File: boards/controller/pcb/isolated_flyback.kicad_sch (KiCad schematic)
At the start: 20 parts, among them T901 150u

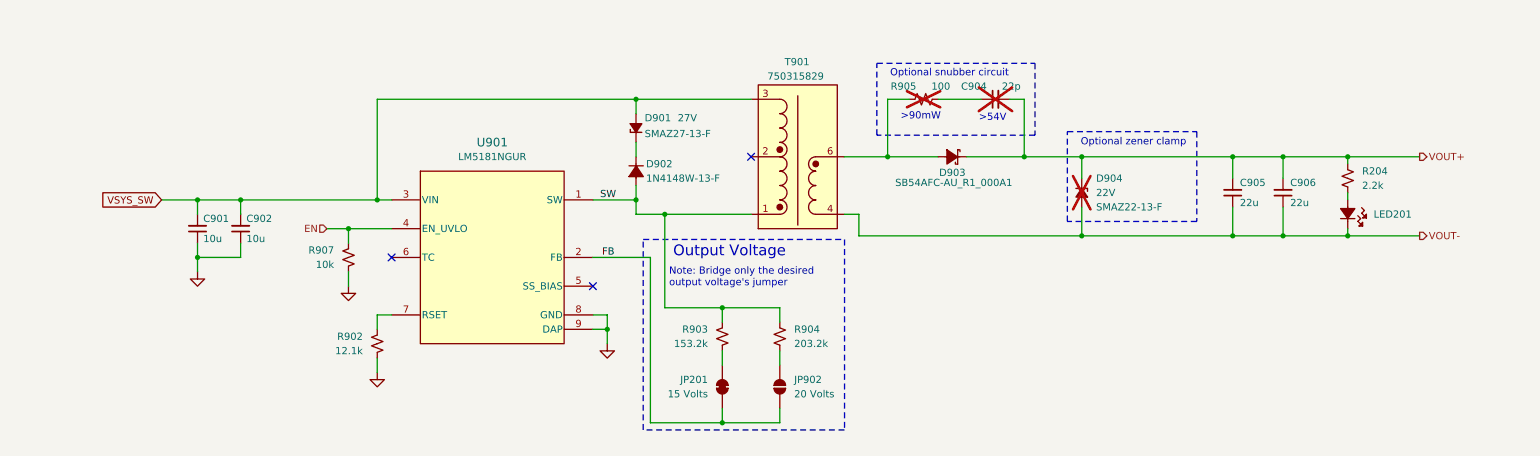
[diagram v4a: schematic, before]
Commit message: controller: pcb: Update schematic
Signed-off-by: Nicholas Loehrke <nicholasnloehrke@gmail.com>
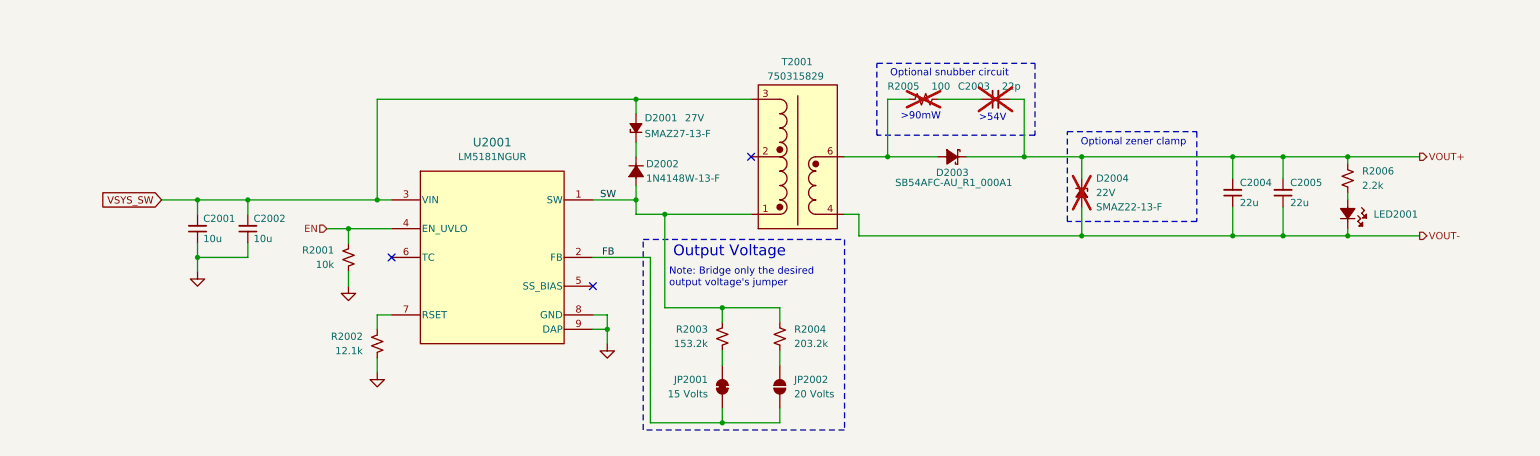
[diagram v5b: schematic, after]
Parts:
- renumbered C901 to C2001, C902 to C2002, C904 to C2003, C905 to C2004, C906 to C2005, D901 to D2001, D902 to D2002, D903 to D2003, D904 to D2004, JP201 to JP2001, JP902 to JP2002, LED201 to LED2001, R907 to R2001, R902 to R2002, R903 to R2003, R904 to R2004, R905 to R2005, R204 to R2006, T901 to T2001, U901 to U2001
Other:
- moved on the sheet: C2002
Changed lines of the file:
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@@
+	)
+	(junction
+		(at 54.61 93.98)
+		(diameter 0)
+		(color 0 0 0 0)
 	)
 	(junction
@@
 	)
 	(junction
-		(at 53.34 93.98)
-		(diameter 0)
-		(color 0 0 0 0)
-	)
-	(junction
 		(at 123.19 93.98)
 		(diameter 0)
@@
 	(wire
 		(pts
-			(xy 53.34 93.98) (xy 77.47 93.98)
-		)
-		(stroke
-			(width 0.508)
-			(type default)
-		)
-	)
-	(wire
-		(pts
 			(xy 138.43 113.03) (xy 128.27 113.03)
 		)
@@
 	(wire
 		(pts
+			(xy 54.61 93.98) (xy 77.47 93.98)
+		)
+		(stroke
+			(width 0.508)
+			(type default)
+		)
+	)
+	(wire
+		(pts
 			(xy 72.39 101.6) (xy 72.39 99.06)
 		)
@@
 	(wire
 		(pts
-			(xy 45.72 104.14) (xy 53.34 104.14)
+			(xy 45.72 104.14) (xy 54.61 104.14)
 		)
 		(stroke
@@
 	(wire
 		(pts
-			(xy 45.72 93.98) (xy 53.34 93.98)
+			(xy 45.72 93.98) (xy 54.61 93.98)
 		)
 		(stroke
@@
 	(wire
 		(pts
-			(xy 53.34 101.6) (xy 53.34 104.14)
+			(xy 54.61 101.6) (xy 54.61 104.14)
 		)
 		(stroke
@@
 	(wire
 		(pts
-			(xy 53.34 93.98) (xy 53.34 96.52)
+			(xy 54.61 93.98) (xy 54.61 96.52)
 		)
 		(stroke
@@
 		(dnp no)
 		(fields_autoplaced yes)
-		(property "Reference" "U901"
+		(property "Reference" "U2001"
 			(at 97.79 83.82 0)
 			(effects
@@
 			(project "controller"
 				(path "/5caba13a-97ae-46d4-856f-900b12012fd8/3c6b0707-a67d-4a65-a38c-f4ab92a2c5a4"
-					(reference "U901")
+					(reference "U2001")
 					(unit 1)
 				)
@@
 		(dnp no)
 		(fields_autoplaced yes)
-		(property "Reference" "#PWR0904"
+		(property "Reference" "#PWR02002"
 			(at 72.39 115.57 0)
 			(effects
@@
 			(project "controller"
 				(path "/5caba13a-97ae-46d4-856f-900b12012fd8/3c6b0707-a67d-4a65-a38c-f4ab92a2c5a4"
-					(reference "#PWR0904")
+					(reference "#PWR02002")
 					(unit 1)
 				)
@@
 		(on_board yes)
 		(dnp no)
-		(property "Reference" "T901"
+		(property "Reference" "T2001"
 			(at 151.638 69.596 0)
 			(effects
@@
 			(project "controller"
 				(path "/5caba13a-97ae-46d4-856f-900b12012fd8/3c6b0707-a67d-4a65-a38c-f4ab92a2c5a4"
-					(reference "T901")
+					(reference "T2001")
 					(unit 1)
 				)
@@
 		(on_board yes)
 		(dnp no)
-		(property "Reference" "D903"
+		(property "Reference" "D2003"
 			(at 179.07 89.154 0)
 			(effects
@@
 			(project "controller"
 				(path "/5caba13a-97ae-46d4-856f-900b12012fd8/3c6b0707-a67d-4a65-a38c-f4ab92a2c5a4"
-					(reference "D903")
+					(reference "D2003")
 					(unit 1)
 				)
@@
 		(on_board yes)
 		(dnp no)
-		(property "Reference" "R902"
+		(property "Reference" "R2002"
 			(at 74.93 118.1099 0)
 			(effects
@@
 			(project "controller"
 				(path "/5caba13a-97ae-46d4-856f-900b12012fd8/3c6b0707-a67d-4a65-a38c-f4ab92a2c5a4"
-					(reference "R902")
+					(reference "R2002")
 					(unit 1)
 				)
@@
 		(on_board yes)
 		(dnp no)
-		(property "Reference" "R903"
+		(property "Reference" "R2003"
 			(at 135.89 116.8399 0)
 			(effects
@@
 			(project "controller"
 				(path "/5caba13a-97ae-46d4-856f-900b12012fd8/3c6b0707-a67d-4a65-a38c-f4ab92a2c5a4"
-					(reference "R903")
+					(reference "R2003")
 					(unit 1)
 				)
@@
 		(dnp no)
 		(fields_autoplaced yes)
-		(property "Reference" "#PWR0901"
+		(property "Reference" "#PWR02001"
 			(at 45.72 113.03 0)
 			(effects
@@
 			(project "controller"
 				(path "/5caba13a-97ae-46d4-856f-900b12012fd8/3c6b0707-a67d-4a65-a38c-f4ab92a2c5a4"
-					(reference "#PWR0901")
+					(reference "#PWR02001")
 					(unit 1)
 				)
@@
 		(dnp no)
 		(fields_autoplaced yes)
-		(property "Reference" "R204"
+		(property "Reference" "R2006"
 			(at 251.46 88.8999 0)
 			(effects
@@
 			(project ""
 				(path "/5caba13a-97ae-46d4-856f-900b12012fd8/3c6b0707-a67d-4a65-a38c-f4ab92a2c5a4"
-					(reference "R204")
+					(reference "R2006")
 					(unit 1)
 				)
@@
 		(on_board yes)
 		(dnp no)
-		(property "Reference" "C905"
+		(property "Reference" "C2004"
 			(at 229.87 90.932 0)
 			(effects
@@
 			(project "controller"
 				(path "/5caba13a-97ae-46d4-856f-900b12012fd8/3c6b0707-a67d-4a65-a38c-f4ab92a2c5a4"
-					(reference "C905")
+					(reference "C2004")
 					(unit 1)
 				)
@@
 		(on_board yes)
 		(dnp yes)
-		(property "Reference" "R905"
+		(property "Reference" "R2005"
 			(at 170.434 73.914 90)
 			(effects
@@
 			(project "controller"
 				(path "/5caba13a-97ae-46d4-856f-900b12012fd8/3c6b0707-a67d-4a65-a38c-f4ab92a2c5a4"
-					(reference "R905")
+					(reference "R2005")
 					(unit 1)
 				)
@@
 		(on_board yes)
 		(dnp no)
-		(property "Reference" "D902"
+		(property "Reference" "D2002"
 			(at 124.968 87.63 90)
 			(effects
@@
 			(project "controller"
 				(path "/5caba13a-97ae-46d4-856f-900b12012fd8/3c6b0707-a67d-4a65-a38c-f4ab92a2c5a4"
-					(reference "D902")
+					(reference "D2002")
 					(unit 1)
 				)
@@
 		(dnp no)
 		(fields_autoplaced yes)
-		(property "Reference" "R904"
+		(property "Reference" "R2004"
 			(at 151.13 116.8399 0)
 			(effects
@@
 			(project "controller"
 				(path "/5caba13a-97ae-46d4-856f-900b12012fd8/3c6b0707-a67d-4a65-a38c-f4ab92a2c5a4"
-					(reference "R904")
+					(reference "R2004")
 					(unit 1)
 				)
@@
 		(on_board yes)
 		(dnp no)
-		(property "Reference" "R907"
+		(property "Reference" "R2001"
 			(at 69.85 102.8699 0)
 			(effects
@@
 			(project "controller"
 				(path "/5caba13a-97ae-46d4-856f-900b12012fd8/3c6b0707-a67d-4a65-a38c-f4ab92a2c5a4"
-					(reference "R907")
+					(reference "R2001")
 					(unit 1)
 				)
@@
 	(symbol
 		(lib_id "Device:C_Small")
-		(at 53.34 99.06 180)
+		(at 54.61 99.06 180)
 		(unit 1)
 		(exclude_from_sim no)
@@
 		(on_board yes)
 		(dnp no)
-		(property "Reference" "C902"
-			(at 54.356 97.282 0)
+		(property "Reference" "C2002"
+			(at 55.626 97.282 0)
 			(effects
 				(font
@@
 		)
 		(property "Value" "10u"
-			(at 54.356 100.838 0)
+			(at 55.626 100.838 0)
 			(effects
 				(font
@@
 		)
 		(property "Footprint" "Capacitor_SMD:C_1206_3216Metric"
-			(at 53.34 99.06 0)
+			(at 54.61 99.06 0)
 			(effects
 				(font
@@
 		)
 		(property "Datasheet" "~"
-			(at 53.34 99.06 0)
+			(at 54.61 99.06 0)
 			(effects
 				(font
@@
 		)
 		(property "Description" "Unpolarized capacitor, small symbol"
-			(at 53.34 99.06 0)
+			(at 54.61 99.06 0)
 			(effects
 				(font
@@
 			(project "controller"
 				(path "/5caba13a-97ae-46d4-856f-900b12012fd8/3c6b0707-a67d-4a65-a38c-f4ab92a2c5a4"
-					(reference "C902")
+					(reference "C2002")
 					(unit 1)
 				)
@@
 		(dnp no)
 		(fields_autoplaced yes)
-		(property "Reference" "#PWR0903"
+		(property "Reference" "#PWR02004"
 			(at 118.11 125.73 0)
 			(effects
@@
 			(project "controller"
 				(path "/5caba13a-97ae-46d4-856f-900b12012fd8/3c6b0707-a67d-4a65-a38c-f4ab92a2c5a4"
-					(reference "#PWR0903")
+					(reference "#PWR02004")
 					(unit 1)
 				)
@@
 		(dnp no)
 		(fields_autoplaced yes)
-		(property "Reference" "#PWR0902"
+		(property "Reference" "#PWR02003"
 			(at 77.47 130.81 0)
 			(effects
@@
 			(project "controller"
 				(path "/5caba13a-97ae-46d4-856f-900b12012fd8/3c6b0707-a67d-4a65-a38c-f4ab92a2c5a4"
-					(reference "#PWR0902")
+					(reference "#PWR02003")
 					(unit 1)
 				)
@@
 		(on_board yes)
 		(dnp no)
-		(property "Reference" "D901"
+		(property "Reference" "D2001"
 			(at 124.714 79.5019 90)
 			(effects
@@
 		)
 		(property "Value" "27V"
-			(at 130.556 79.502 90)
+			(at 131.826 79.502 90)
 			(effects
 				(font
@@
 			(project "controller"
 				(path "/5caba13a-97ae-46d4-856f-900b12012fd8/3c6b0707-a67d-4a65-a38c-f4ab92a2c5a4"
-					(reference "D901")
+					(reference "D2001")
 					(unit 1)
 				)
@@
 		(on_board yes)
 		(dnp yes)
-		(property "Reference" "C904"
+		(property "Reference" "C2003"
 			(at 182.88 73.914 90)
 			(effects
@@
 			(project "controller"
 				(path "/5caba13a-97ae-46d4-856f-900b12012fd8/3c6b0707-a67d-4a65-a38c-f4ab92a2c5a4"
-					(reference "C904")
+					(reference "C2003")
 					(unit 1)
 				)
@@
 		(on_board yes)
 		(dnp no)
-		(property "Reference" "LED201"
+		(property "Reference" "LED2001"
 			(at 253.492 96.52 90)
 			(effects
@@
 			(project ""
 				(path "/5caba13a-97ae-46d4-856f-900b12012fd8/3c6b0707-a67d-4a65-a38c-f4ab92a2c5a4"
-					(reference "LED201")
+					(reference "LED2001")
 					(unit 1)
 				)
@@
 		(on_board yes)
 		(dnp no)
-		(property "Reference" "JP201"
+		(property "Reference" "JP2001"
 			(at 135.89 125.7299 90)
 			(effects
@@
 			(project ""
 				(path "/5caba13a-97ae-46d4-856f-900b12012fd8/3c6b0707-a67d-4a65-a38c-f4ab92a2c5a4"
-					(reference "JP201")
+					(reference "JP2001")
 					(unit 1)
 				)
@@
 		(on_board yes)
 		(dnp yes)
-		(property "Reference" "D904"
+		(property "Reference" "D2004"
 			(at 204.47 90.1699 90)
 			(effects
@@
 			(project "controller"
 				(path "/5caba13a-97ae-46d4-856f-900b12012fd8/3c6b0707-a67d-4a65-a38c-f4ab92a2c5a4"
-					(reference "D904")
+					(reference "D2004")
 					(unit 1)
 				)
@@
 		(on_board yes)
 		(dnp no)
-		(property "Reference" "C906"
+		(property "Reference" "C2005"
 			(at 238.76 90.932 0)
 			(effects
@@
 			(project "controller"
 				(path "/5caba13a-97ae-46d4-856f-900b12012fd8/3c6b0707-a67d-4a65-a38c-f4ab92a2c5a4"
-					(reference "C906")
+					(reference "C2005")
 					(unit 1)
 				)
@@
 		(on_board yes)
 		(dnp no)
-		(property "Reference" "C901"
+		(property "Reference" "C2001"
 			(at 46.736 97.282 0)
 			(effects
@@
 			(project "controller"
 				(path "/5caba13a-97ae-46d4-856f-900b12012fd8/3c6b0707-a67d-4a65-a38c-f4ab92a2c5a4"
-					(reference "C901")
+					(reference "C2001")
 					(unit 1)
 				)
@@
 		(dnp no)
 		(fields_autoplaced yes)
-		(property "Reference" "JP902"
+		(property "Reference" "JP2002"
 			(at 151.13 125.7299 90)
 			(effects
@@
 			(project "controller"
 				(path "/5caba13a-97ae-46d4-856f-900b12012fd8/3c6b0707-a67d-4a65-a38c-f4ab92a2c5a4"
-					(reference "JP902")
+					(reference "JP2002")
 					(unit 1)
 				)

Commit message: controller: pcb: Update schematic
- Replace 22u caps with 10u since 22u are very expensive
- Add TCC and MPN fields

Signed-off-by: Nicholas Loehrke <nicholasnloehrke@gmail.com>
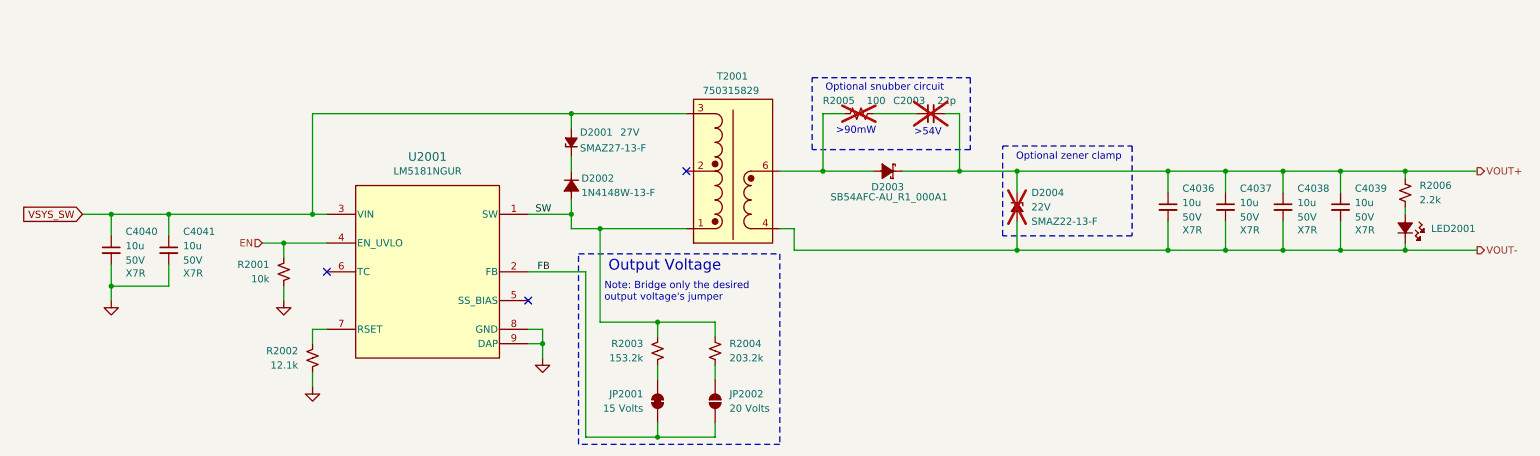
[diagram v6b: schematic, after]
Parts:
- removed C2001, C2002: 10u, Capacitor_SMD:C_1206_3216Metric, symbol Device:C_Small
- removed C2004: 22u, Capacitor_SMD:C_0805_2012Metric, symbol Device:C_Small
- removed C2005: 22u, Capacitor_SMD:C_1206_3216Metric, symbol Device:C_Small
- added C4036, C4037, C4038, C4039, C4040, C4041: 10u, symbol Device:C_Small
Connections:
- net GND: now also C4040.2, C4041.2
- net VOUT+: now also C4036.1, C4037.1, C4038.1, C4039.1
- net VOUT-: now also C4036.2, C4037.2, C4038.2, C4039.2
- net VSYS_SW: now also C4040.1, C4041.1
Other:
- moved on the sheet: C2003, D2001, D2002, D2003, D2004, JP2001, JP2002, LED2001, R2001, R2002, R2003, R2004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

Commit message: controller: pcb: Update schematic
- Add TVS diodes on select MCU pins

Signed-off-by: Nicholas Loehrke <nicholasnloehrke@gmail.com>
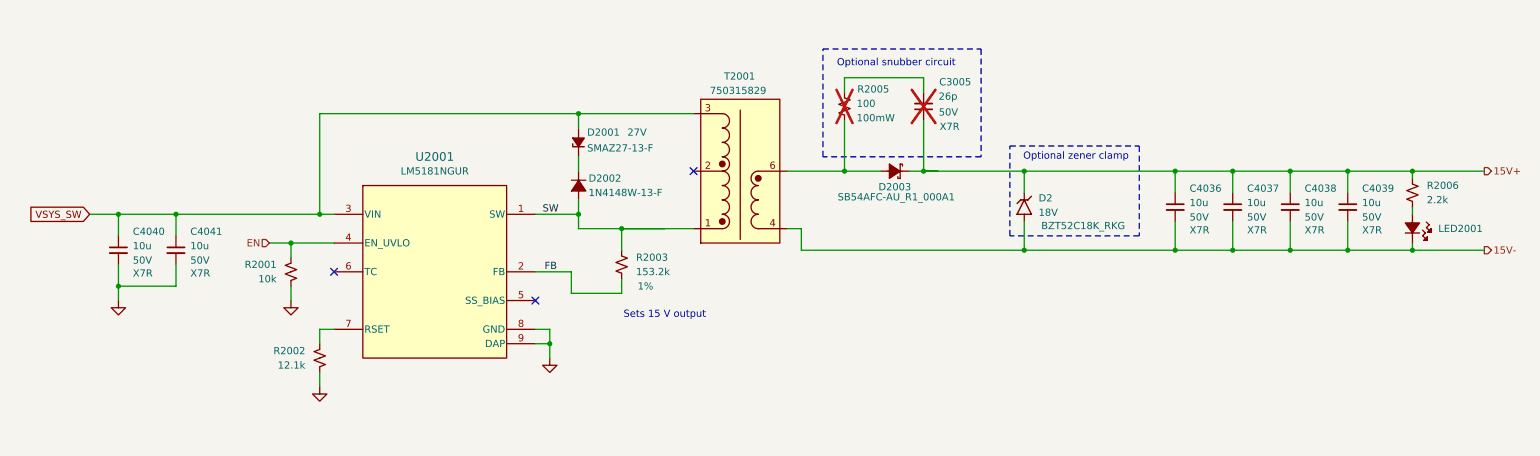
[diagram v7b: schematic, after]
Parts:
- removed C2003: 22p, Capacitor_SMD:C_0603_1608Metric, symbol Device:C_Small
- removed D2004: 22V, SMAZ22-13-F:SMAZ22-13-F, symbol SMAZ22-13-F:SMAZ22-13-F
- removed JP2001: 15 Volts, symbol Jumper:SolderJumper_2_Bridged
- removed JP2002: 20 Volts, Jumper:SolderJumper-2_P1.3mm_Open_RoundedPad1.0x1.5mm, symbol Jumper:SolderJumper_2_Open
- removed R2004: 203.2k, Resistor_SMD:R_0603_1608Metric, symbol Device:R_Small_US
- added C3005: 26p, symbol Device:C_Small
- added D2: 18V, BZT52C18K_RKG:DIO_BZT52C18K_RKG, symbol BZT52C18K_RKG:BZT52C18K_RKG
- R2003: Tolerance (none) -> 1%
- R2005: Power (none) -> 100mW
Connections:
- net FB: now also R2003.2
- net at D2003.2, T2001.6: now also R2005.2; no longer R2005.1
- net VOUT+ renamed 15V+
- net 15V+: now also C3005.1, D2.C
- net VOUT- renamed 15V-
- net 15V-: now also D2.A
- new net: C3005.2, R2005.1
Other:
- note added: "Sets 15 V output"
- note removed: ">54V"
- note removed: ">90mW"
- note removed: "Note: Bridge only the desired output voltage's jumper"
- note removed: "Output Voltage"
- moved on the sheet: C4036, C4037, C4038, C4039, C4040, C4041, D2001, D2002, D2003, LED2001, R2001, R2002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

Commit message: controller: pcb: Update schematic
Signed-off-by: Nicholas Loehrke <nicholasnloehrke@gmail.com>
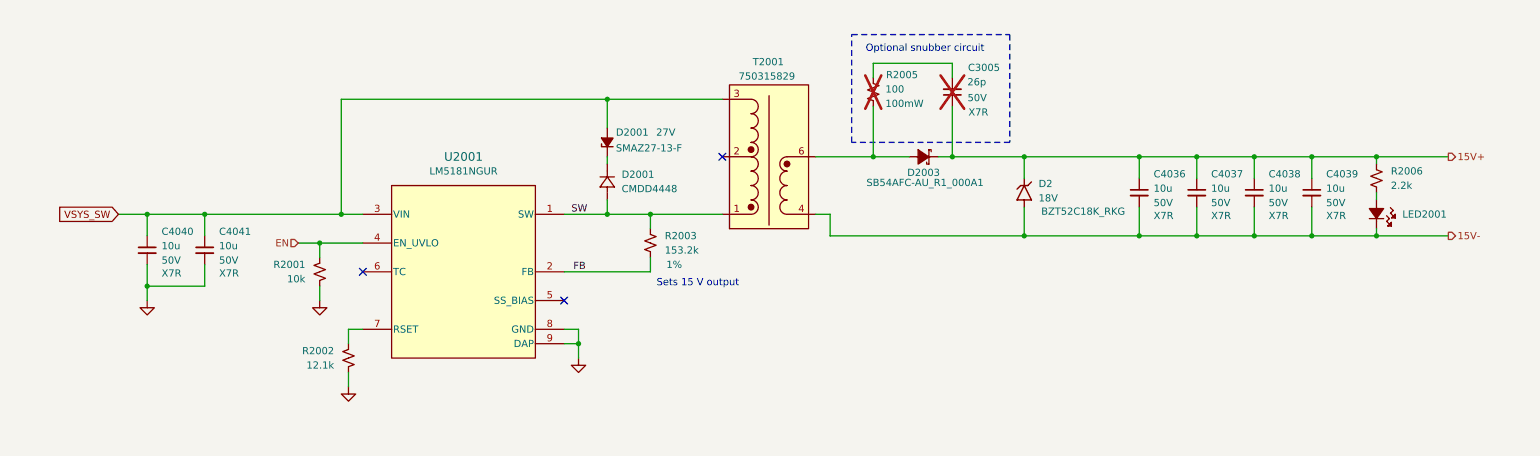
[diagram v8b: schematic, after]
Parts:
- removed D2002: ~, 1N4148W-13-F:1N4148W-13-F, symbol 1N4148W-13-F:1N4148W-13-F
- added D2001: CMDD4448, SOD-323_CNS, symbol CMDD4448:CMDD4448_TR_PBFREE
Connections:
- net SW: now also D2001.2
- net at D2001.1 (K): now also D2001.1
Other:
- note removed: "Optional zener clamp"
- moved on the sheet: C3005, C4036, C4037, C4038, C4039, C4040, C4041, D2, D2001, D2003, LED2001, R2001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
